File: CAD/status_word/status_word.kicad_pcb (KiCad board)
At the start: 2 copper layers, 0 parts

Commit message: add Status Word PCB, not finished
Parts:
- added C1: 100nF, Capacitor_SMD:C_0805_2012Metric, F.Cu at (78.7, 69.5)
- added C2: 100nF, Capacitor_SMD:C_0805_2012Metric, F.Cu at (95.2, 69.5)
- added C3: 100nF, Capacitor_SMD:C_0805_2012Metric, F.Cu at (65.1, 55.0)
- added C4: 100nF, Capacitor_SMD:C_0805_2012Metric, F.Cu at (80.5, 53.2)
- added C5: 100nF, Capacitor_SMD:C_0805_2012Metric, F.Cu at (103.0, 52.5)
- added C6: 100nF, Capacitor_SMD:C_0805_2012Metric, F.Cu at (120.7, 60.9)
- added C7: 10uF, Capacitor_SMD:C_0805_2012Metric, F.Cu at (63.5, 42.2)
- added D1: ZF, LED_SMD:LED_0805_2012Metric, F.Cu at (98.1, 47.0)
- added D10: STI, LED_SMD:LED_0805_2012Metric, F.Cu at (71.4, 74.3)
- added D2: CF, LED_SMD:LED_0805_2012Metric, F.Cu at (103.2, 47.0)
- added D3: NF, LED_SMD:LED_0805_2012Metric, F.Cu at (108.3, 47.0)
- added D4: VF, LED_SMD:LED_0805_2012Metric, F.Cu at (113.4, 47.0)
- added D5: IM, LED_SMD:LED_0805_2012Metric, F.Cu at (118.4, 47.0)
- added D6: SW_IN, LED_SMD:LED_0805_2012Metric, F.Cu at (70.9, 42.4)
- added D7: SW_OUT, LED_SMD:LED_0805_2012Metric, F.Cu at (85.8, 42.4)
- added D8: L_FLAGS, LED_SMD:LED_0805_2012Metric, F.Cu at (103.5, 68.6)
- added D9: CLI, LED_SMD:LED_0805_2012Metric, F.Cu at (86.6, 74.3)
- added J1: Conn_SW, Connector_PinHeader_2.54mm:PinHeader_2x13_P2.54mm_Horizontal, F.Cu at (59.7, 73.7)
- added R1: 1k, Resistor_SMD:R_0805_2012Metric, F.Cu at (98.1, 43.2)
- added R10: 1k, Resistor_SMD:R_0805_2012Metric, F.Cu at (75.3, 74.3)
- added R2: 1k, Resistor_SMD:R_0805_2012Metric, F.Cu at (103.2, 43.2)
- added R3: 1k, Resistor_SMD:R_0805_2012Metric, F.Cu at (108.3, 43.2)
- added R4: 1k, Resistor_SMD:R_0805_2012Metric, F.Cu at (113.4, 43.2)
- added R5: 1k, Resistor_SMD:R_0805_2012Metric, F.Cu at (118.5, 43.2)
- added R6: 1k, Resistor_SMD:R_0805_2012Metric, F.Cu at (74.8, 42.4)
- added R7: 1k, Resistor_SMD:R_0805_2012Metric, F.Cu at (89.9, 42.4)
- added R8: 1k, Resistor_SMD:R_0805_2012Metric, F.Cu at (107.3, 68.6)
- added R9: 1k, Resistor_SMD:R_0805_2012Metric, F.Cu at (90.5, 74.3)
- added U1: AFLAGS, Package_SO:SO-16_3.9x9.9mm_P1.27mm, F.Cu at (71.8, 66.1)
- added U2: IMASK, Package_SO:SO-16_3.9x9.9mm_P1.27mm, F.Cu at (88.3, 66.1)
- added U3: MUX1, Package_SO:SO-16_3.9x9.9mm_P1.27mm, F.Cu at (71.8, 55.9)
- added U4: MUX2, Package_SO:SO-16_3.9x9.9mm_P1.27mm, F.Cu at (88.3, 55.9)
- added U5: BUFFER, Package_SO:SO-20_5.3x12.6mm_P1.27mm, F.Cu at (111.1, 56.9)
- added U6: 74HC02, Package_SO:SO-14_3.9x8.65mm_P1.27mm, F.Cu at (118.0, 67.7)
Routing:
- net +5V: track 0.00 -> 205.0 mm, vias 0 -> 6
- net /sw.im: track 0.00 -> 102.0 mm, vias 0 -> 4
- net /sw.vf: track 0.00 -> 95.6 mm, vias 0 -> 4
- net sw_in: track 0.00 -> 87.0 mm, vias 0 -> 3
- net /sw.nf: track 0.00 -> 85.5 mm, vias 0 -> 4
- net /sw.cf: track 0.00 -> 81.4 mm, vias 0 -> 4
- net aflags_in: track 0.00 -> 81.0 mm
- net ~{sw_out}: track 0.00 -> 75.6 mm, vias 0 -> 3
- net /sw.zf: track 0.00 -> 71.4 mm, vias 0 -> 2
- net cli: track 0.00 -> 68.3 mm
- net /dbus4: track 0.00 -> 67.9 mm, vias 0 -> 2
- net /dbus6: track 0.00 -> 65.4 mm, vias 0 -> 1
- net /dbus7: track 0.00 -> 63.7 mm, vias 0 -> 1
- net /dbus2: track 0.00 -> 61.7 mm, vias 0 -> 2
- net /dbus3: track 0.00 -> 60.8 mm, vias 0 -> 2
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- added copper zone on B.Cu, net GND
- added copper zone on F.Cu, net GND
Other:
- board outline added: 70 x 39 mm
- board text added: "AFLAGS_IN"
- board text added: "CF"
- board text added: "CLI"
- board text added: "IM"
- board text added: "NF"
- board text added: "Rev ${REVISION} ${YEAR}/${MONTH}"
- board text added: "STATUS WORD"
- board text added: "STI"
- board text added: "SW_IN"
- board text added: "SW_OUT"
- board text added: "VF"
- board text added: "ZF"

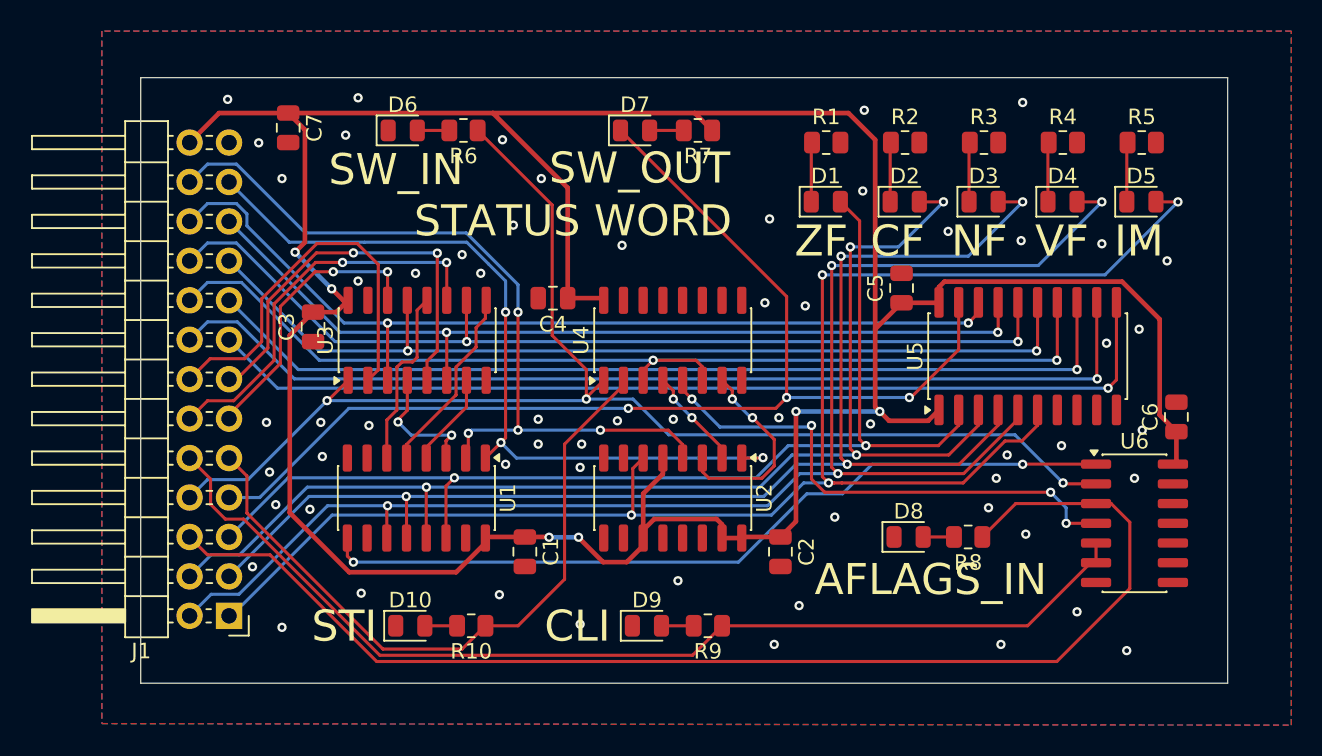
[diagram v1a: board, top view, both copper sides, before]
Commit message: add mounting holes, pull-up, test points in SW
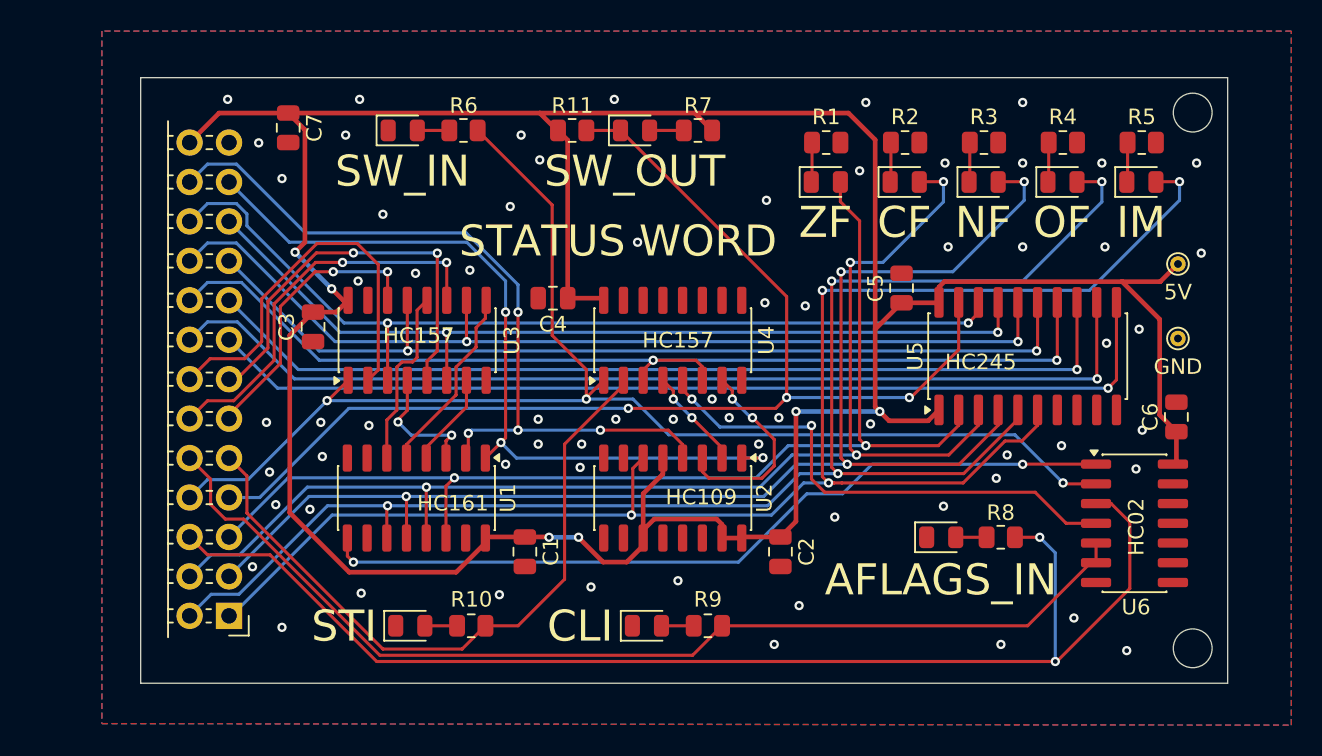
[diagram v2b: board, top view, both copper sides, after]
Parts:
- added R11: 10k, Resistor_SMD:R_0805_2012Metric, F.Cu at (81.8, 42.4)
- added TP1: TestPoint, TestPoint:TestPoint_THTPad_D1.0mm_Drill0.5mm, F.Cu at (120.8, 51.0)
- added TP2: TestPoint, TestPoint:TestPoint_THTPad_D1.0mm_Drill0.5mm, F.Cu at (120.8, 55.8)
- moved R8 2.10 mm to (109.4, 68.6)
- moved D8 2.10 mm to (105.6, 68.6)
- moved D1 1.27 mm to (98.1, 45.7)
- moved D2 1.27 mm to (103.2, 45.7)
- moved D3 1.27 mm to (108.3, 45.7)
- moved D4 1.27 mm to (113.4, 45.7)
- moved D5 1.27 mm to (118.4, 45.7)
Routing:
- net +5V: track 205.0 -> 207.8 mm
- net ~{sw_out}: track 75.6 -> 77.8 mm
- net aflags_in: track 81.0 -> 82.8 mm, vias 0 -> 2
- net /sw.zf: track 71.4 -> 72.7 mm
- net Net-(D1-K): track 3.83 -> 2.63 mm
- net Net-(D4-K): track 3.83 -> 2.63 mm
- net Net-(D3-K): track 3.83 -> 2.63 mm
- net Net-(D2-K): track 3.83 -> 2.63 mm
- net Net-(D5-K): track 3.83 -> 2.63 mm
- net /sw.nf: track 85.5 -> 86.4 mm
- net /sw.im: track 102.0 -> 102.8 mm
- net /sw.cf: track 81.4 -> 82.3 mm
- net /sw.vf: track 95.6 -> 96.3 mm
- net Net-(U4-I0b): track 33.5 -> 32.9 mm, vias 4 -> 2
- net GND: vias 60 -> 67
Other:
- outline, holes or cut-outs redrawn
- board text added: "5V"
- board text added: "GND"
- board text added: "HC02"
- board text added: "HC109"
- board text added: "HC157"
- board text added: "HC161"
- board text added: "HC245"
- board text added: "OF"
- board text removed: "VF"

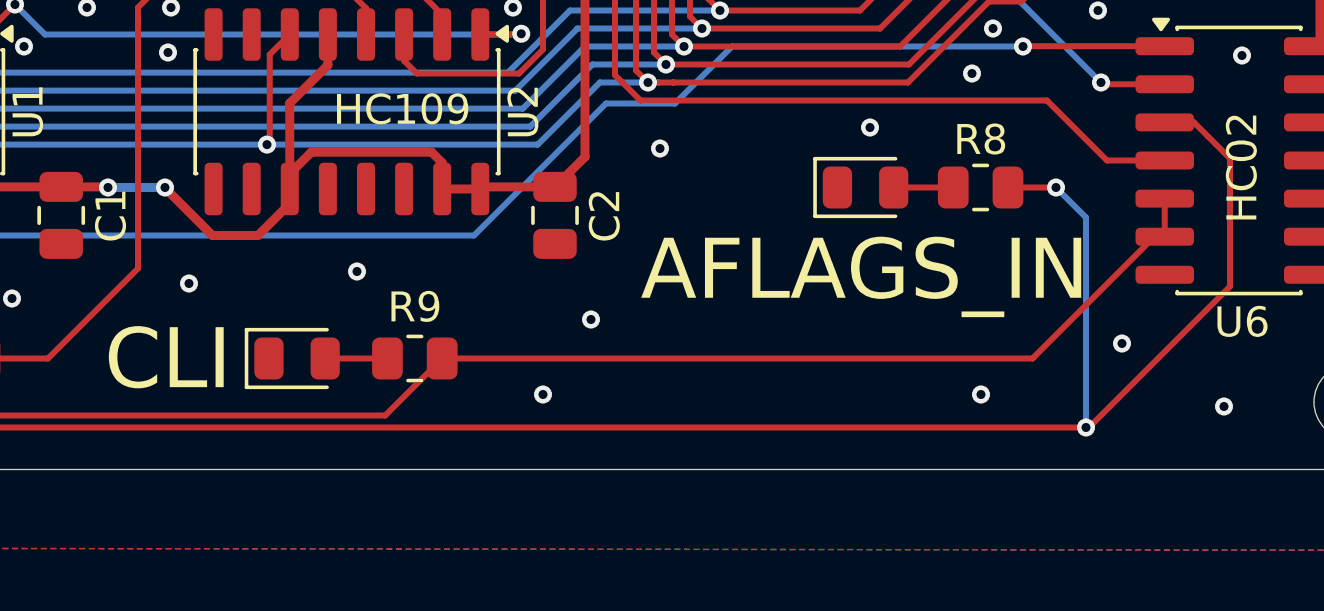
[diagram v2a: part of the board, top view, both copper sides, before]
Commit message: update silkscreen qr code, license, add images
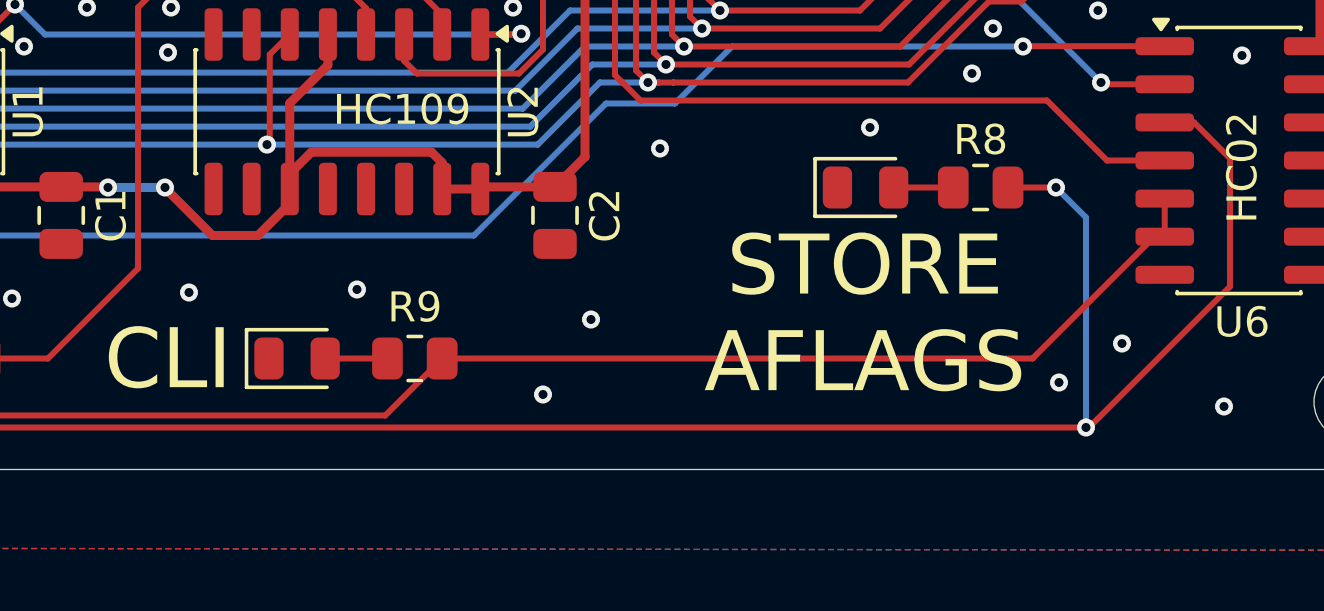
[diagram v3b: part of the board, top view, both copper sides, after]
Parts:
- added G***: Github QR Code, LOGO, B.Cu at (103.5, 71.5)
- added Ref**: Val**, 8-bit_computer:by-nc-sa.eu, B.Cu at (85.3, 68.0)
- J1: value Conn_SW -> Conn_01x26_Pin
- U1: value AFLAGS -> 74HC161
- U2: value IMASK -> 74HC109
- U3: value MUX1 -> 74HC157
- U4: value MUX2 -> 74HC157
- U5: value BUFFER -> 74HC245
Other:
- board text added: "STORE AFLAGS"
- board text removed: "AFLAGS_IN"

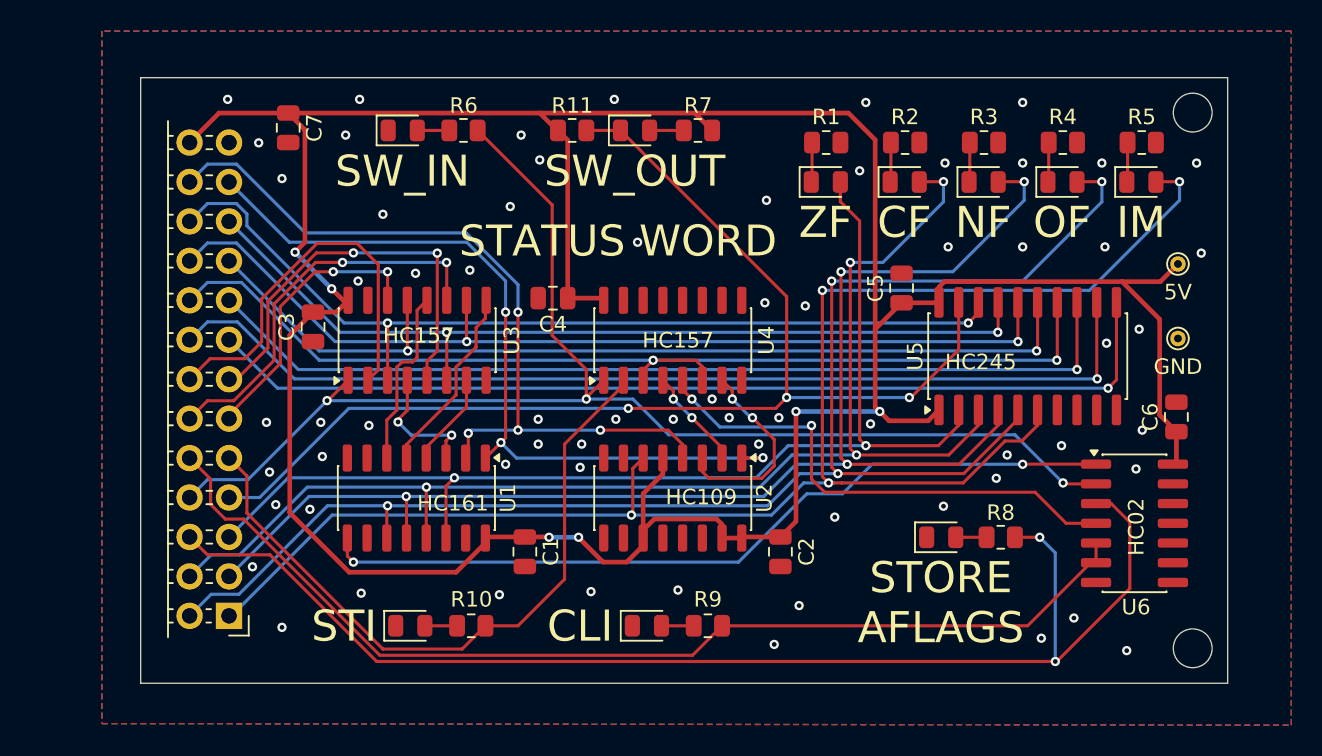
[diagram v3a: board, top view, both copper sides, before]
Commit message: add tooling holes to SW, update libraries
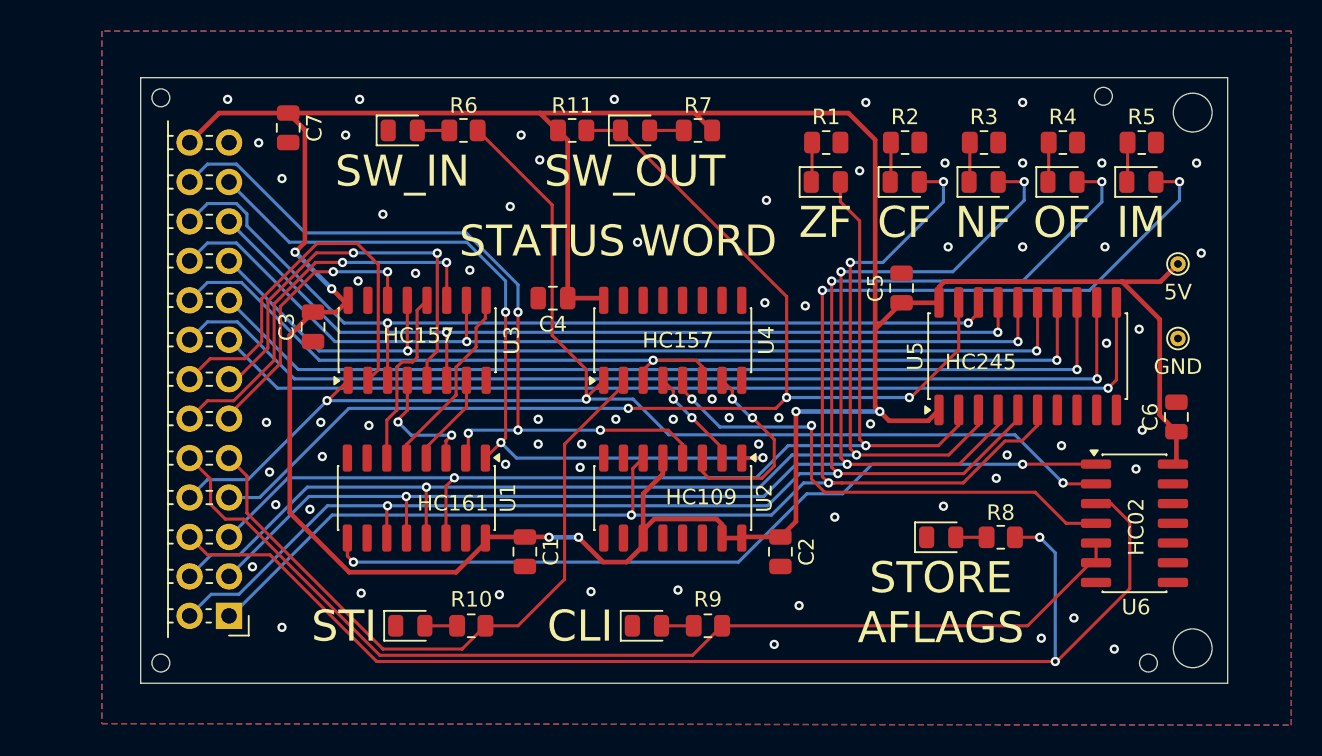
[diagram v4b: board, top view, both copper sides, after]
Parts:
- added REF**: ToolingHole_1.152mm, MountingHole:ToolingHole_1.152mm, F.Cu at (55.3, 76.7)
- added REF**: ToolingHole_1.152mm, MountingHole:ToolingHole_1.152mm, F.Cu at (118.9, 76.7)
- added REF**: ToolingHole_1.152mm, MountingHole:ToolingHole_1.152mm, F.Cu at (55.3, 40.3)
- added REF**: ToolingHole_1.152mm, MountingHole:ToolingHole_1.152mm, F.Cu at (116.0, 40.2)

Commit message: layout changes, adding mounting holes, modifying tooling holes and adding fiducials
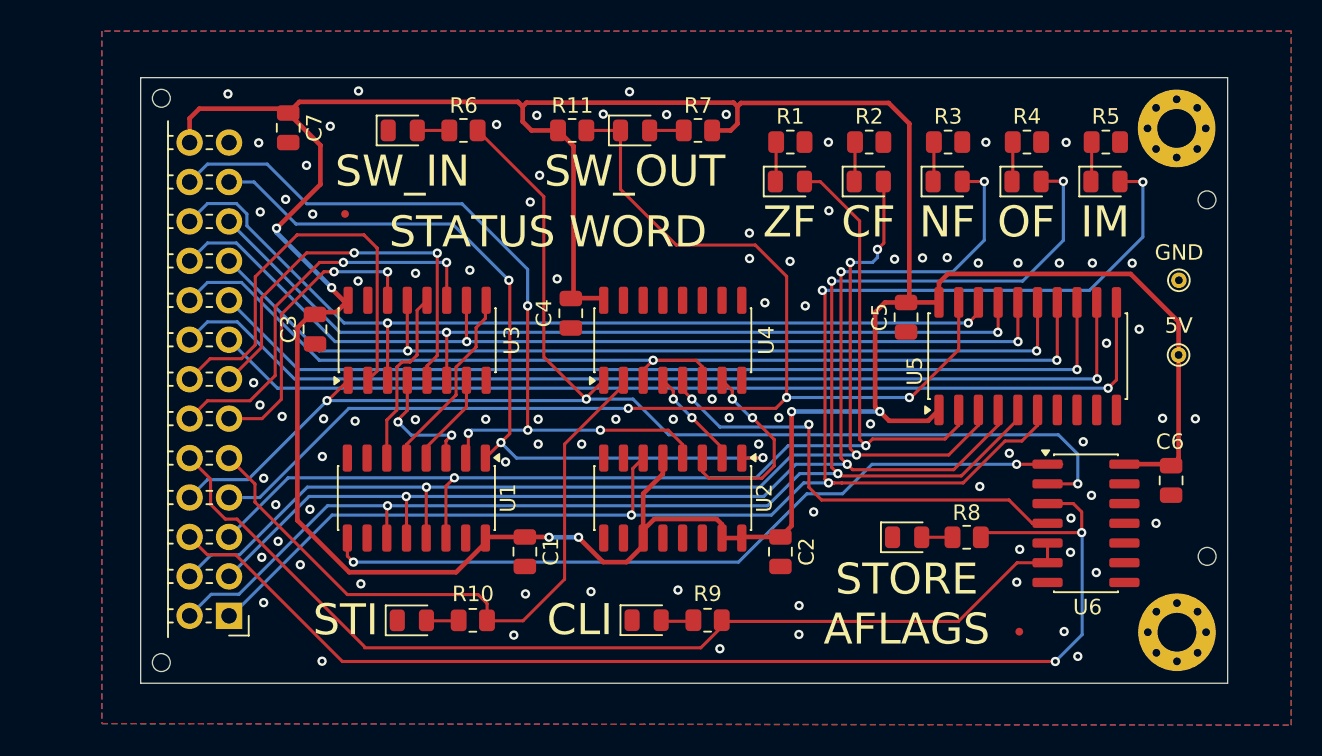
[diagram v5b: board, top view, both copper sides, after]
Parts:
- removed REF** (x4): ToolingHole_1.152mm, MountingHole:ToolingHole_1.152mm
- removed Ref**: Val**, 8-bit_computer:by-nc-sa.eu
- added FID1: Fiducial, Fiducial:Fiducial_0.5mm_Mask1mm, F.Cu at (67.2, 47.8)
- added FID2: Fiducial, Fiducial:Fiducial_0.5mm_Mask1mm, F.Cu at (110.6, 74.7)
- added H1: MountingHole_Pad, MountingHole:MountingHole_2.5mm_Pad_Via, F.Cu at (120.7, 42.3)
- added H2: MountingHole_Pad, MountingHole:MountingHole_2.5mm_Pad_Via, F.Cu at (120.7, 74.7)
- added H3: ToolingHole, MountingHole:ToolingHole_1.152mm, F.Cu at (55.3, 40.3)
- added H4: ToolingHole, MountingHole:ToolingHole_1.152mm, F.Cu at (55.3, 76.7)
- added H5: ToolingHole, MountingHole:ToolingHole_1.152mm, F.Cu at (122.7, 46.9)
- added H6: ToolingHole, MountingHole:ToolingHole_1.152mm, F.Cu at (122.7, 69.8)
- moved G*** 28.5 mm to (86.4, 48.6)
- moved TP1 5.86 mm to (120.8, 56.9)
- moved C6 4.10 mm to (120.4, 64.9), turned to -90 degrees
- moved TP2 3.75 mm to (120.9, 52.0)
- moved U6 3.12 mm to (114.9, 67.7)
- moved D1 2.31 mm to (95.8, 45.7)
- moved D2 2.31 mm to (100.9, 45.7)
- moved D3 2.31 mm to (106.0, 45.7)
- moved D4 2.31 mm to (111.0, 45.7)
- moved D5 2.31 mm to (116.1, 45.7)
- moved R1 2.31 mm to (95.8, 43.1)
- moved R2 2.31 mm to (100.9, 43.1)
- moved R3 2.31 mm to (106.0, 43.1)
- moved R4 2.31 mm to (111.1, 43.1)
- moved R5 2.31 mm to (116.2, 43.1)
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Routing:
- net +5V: track 207.8 -> 213.6 mm
- net aflags_in: track 82.8 -> 78.1 mm
- net /sw.cf: track 82.3 -> 78.0 mm
- net cli: track 68.3 -> 64.3 mm
- net Net-(U4-I0b): track 32.9 -> 29.6 mm
- net ~{sw_out}: track 77.8 -> 80.8 mm
- net Net-(U1-~{PE}): track 52.2 -> 49.9 mm
- net /aflags.zf: track 25.7 -> 27.6 mm
- net sw_in: track 87.0 -> 88.9 mm
- net sti: track 44.3 -> 42.6 mm
- net /sw.vf: track 96.3 -> 94.6 mm
- net /sw.zf: track 72.7 -> 74.3 mm
- net /sw.im: track 102.8 -> 101.6 mm
- net /sw.nf: track 86.4 -> 85.4 mm
- net clk: track 51.0 -> 52.0 mm
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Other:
- outline, holes or cut-outs redrawn
- board text added: "S/N"
- board text added: "github.com/${GITHUB}"
- board text removed: "HC02"
- board text removed: "HC109"
- board text removed: "HC157"
- board text removed: "HC161"
- board text removed: "HC245"
